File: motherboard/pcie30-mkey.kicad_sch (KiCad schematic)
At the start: 57 parts, among them IC1 PI6C557-05BLE, J15 Bus_M.2_Socket_M, U20 TPS54331DR, U21 AP2127K-3.3, Y1 25MHz

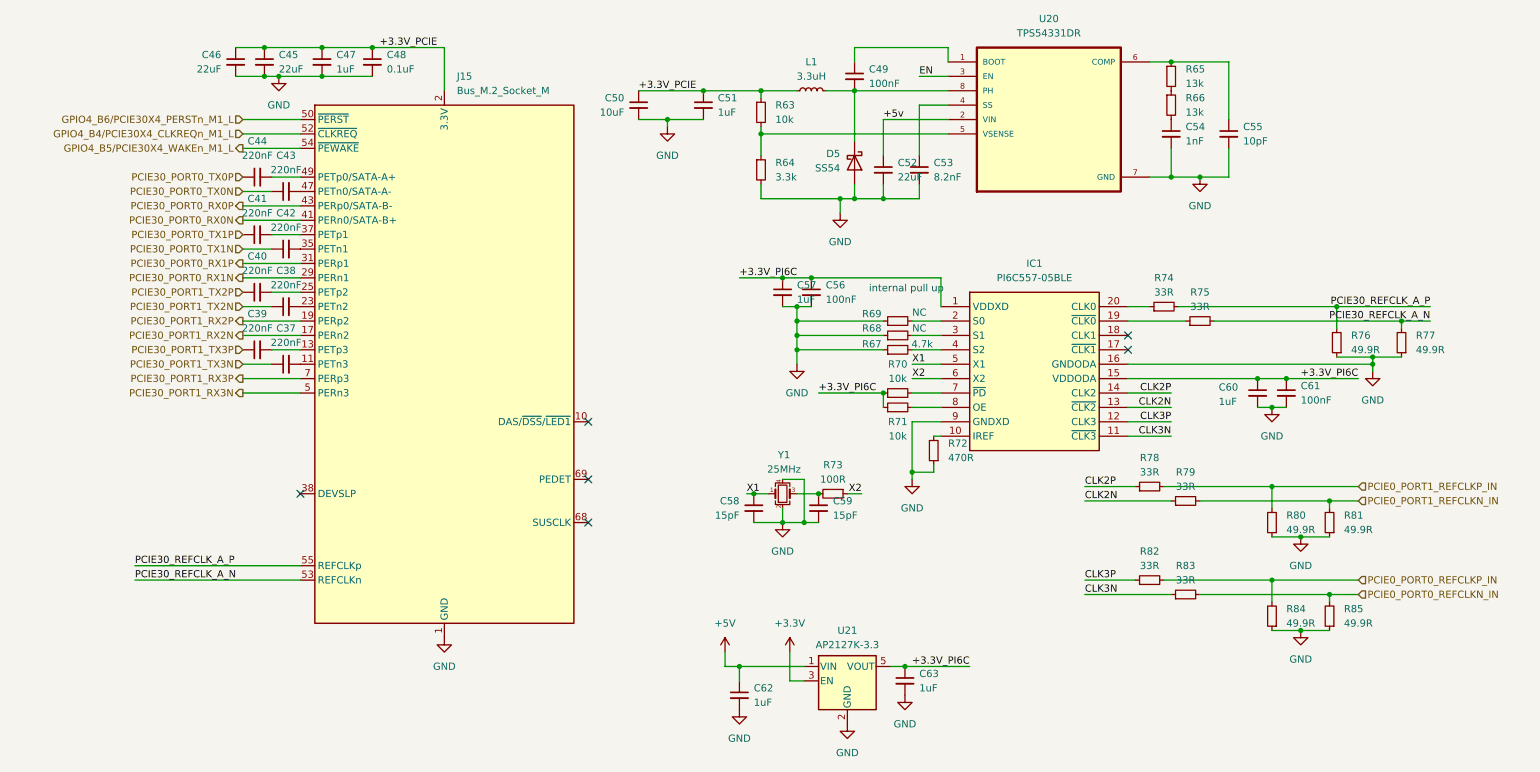
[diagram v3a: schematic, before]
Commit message: cost optimizations for jlc
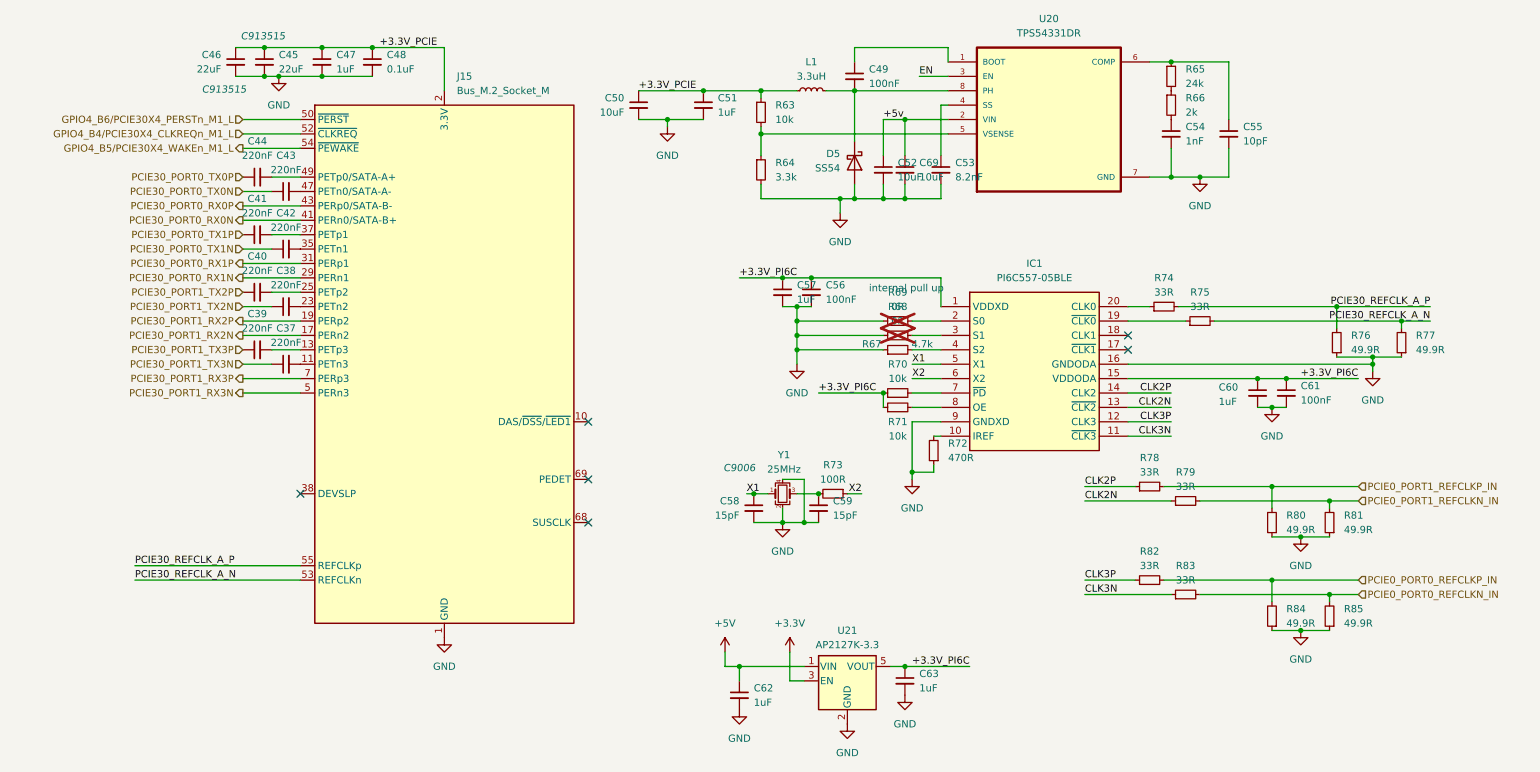
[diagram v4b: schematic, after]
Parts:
- added C69: 10uF, Capacitor_SMD:C_0402_1005Metric, symbol Device:C_Small
- C45, C46: footprint Capacitor_SMD:C_0402_1005Metric -> Capacitor_SMD:C_0603_1608Metric
- C50, C51: footprint Capacitor_SMD:C_1206_3216Metric -> Capacitor_SMD:C_0402_1005Metric
- C52: value 22uF -> 10uF; footprint Capacitor_SMD:C_0603_1608Metric -> Capacitor_SMD:C_0402_1005Metric
- C53: footprint Capacitor_SMD:C_0603_1608Metric -> Capacitor_SMD:C_0402_1005Metric
- R65: value 13k -> 24k
- R66: value 13k -> 2k
- R68, R69: value NC -> 0R; now not fitted
- Y1: footprint Crystal:Crystal_SMD_2016-4Pin_2.0x1.6mm -> Crystal:Crystal_SMD_3225-4Pin_3.2x2.5mm
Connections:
- net +5v: now also C69.1
- net GND: now also C69.2
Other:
- moved on the sheet: C53
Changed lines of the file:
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@@
 	)
 	(junction
+		(at 168.91 46.99)
+		(diameter 0)
+		(color 0 0 0 0)
+	)
+	(junction
 		(at 149.86 66.04)
 		(diameter 0)
@@
 	)
 	(junction
+		(at 168.91 33.02)
+		(diameter 0)
+		(color 0 0 0 0)
+	)
+	(junction
 		(at 139.7 129.54)
 		(diameter 0)
@@
 	(wire
 		(pts
-			(xy 176.53 30.48) (xy 171.45 30.48)
+			(xy 175.26 30.48) (xy 176.53 30.48)
 		)
 		(stroke
@@
 	(wire
 		(pts
+			(xy 168.91 44.45) (xy 168.91 46.99)
+		)
+		(stroke
+			(width 0)
+			(type default)
+		)
+	)
+	(wire
+		(pts
 			(xy 165.1 46.99) (xy 165.1 44.45)
 		)
@@
 	(wire
 		(pts
+			(xy 168.91 33.02) (xy 176.53 33.02)
+		)
+		(stroke
+			(width 0)
+			(type default)
+		)
+	)
+	(wire
+		(pts
+			(xy 168.91 33.02) (xy 168.91 39.37)
+		)
+		(stroke
+			(width 0)
+			(type default)
+		)
+	)
+	(wire
+		(pts
 			(xy 214.63 97.79) (xy 233.68 97.79)
 		)
@@
 	(wire
 		(pts
-			(xy 171.45 30.48) (xy 171.45 39.37)
+			(xy 175.26 30.48) (xy 175.26 39.37)
 		)
 		(stroke
@@
 	(wire
 		(pts
+			(xy 168.91 46.99) (xy 175.26 46.99)
+		)
+		(stroke
+			(width 0)
+			(type default)
+		)
+	)
+	(wire
+		(pts
 			(xy 160.02 36.83) (xy 160.02 27.94)
 		)
@@
 	(wire
 		(pts
-			(xy 165.1 46.99) (xy 171.45 46.99)
+			(xy 165.1 46.99) (xy 168.91 46.99)
 		)
 		(stroke
@@
 	(wire
 		(pts
-			(xy 171.45 46.99) (xy 171.45 44.45)
+			(xy 175.26 46.99) (xy 175.26 44.45)
 		)
 		(stroke
@@
 	(wire
 		(pts
-			(xy 165.1 33.02) (xy 176.53 33.02)
+			(xy 165.1 33.02) (xy 168.91 33.02)
 		)
 		(stroke
@@
 			)
 		)
-		(property "Value" "13k"
+		(property "Value" "2k"
 			(at 218.44 31.7499 0)
 			(effects
@@
 	)
 	(symbol
+		(lib_id "Device:C_Small")
+		(at 168.91 41.91 0)
+		(unit 1)
+		(exclude_from_sim no)
+		(in_bom yes)
+		(on_board yes)
+		(dnp no)
+		(property "Reference" "C69"
+			(at 171.45 40.6462 0)
+			(effects
+				(font
+					(size 1.27 1.27)
+				)
+				(justify left)
+			)
+		)
+		(property "Value" "10uF"
+			(at 171.45 43.18 0)
+			(effects
+				(font
+					(size 1.27 1.27)
+				)
+				(justify left)
+			)
+		)
+		(property "Footprint" "Capacitor_SMD:C_0402_1005Metric"
+			(at 168.91 41.91 0)
+			(effects
+				(font
+					(size 1.27 1.27)
+				)
+				(hide yes)
+			)
+		)
+		(property "Datasheet" "~"
+			(at 168.91 41.91 0)
+			(effects
+				(font
+					(size 1.27 1.27)
+				)
+				(hide yes)
+			)
+		)
+		(property "Description" "C527590"
+			(at 168.91 41.91 0)
+			(effects
+				(font
+					(size 1.27 1.27)
+				)
+				(hide yes)
+			)
+		)
+		(pin "1"
+		)
+		(pin "2"
+		)
+		(instances
+			(project "motherboard"
+				(path "/025fe4d1-0305-4b34-be04-f8d9818125a4/8b9107a7-7899-4235-bab8-96db30f71454"
+					(reference "C69")
+					(unit 1)
+				)
+			)
+		)
+	)
+	(symbol
 		(lib_id "Device:L_Small")
 		(at 152.4 27.94 90)
@@
 		(on_board yes)
 		(dnp no)
-		(fields_autoplaced yes)
 		(property "Reference" "Y1"
 			(at 147.574 92.202 0)
@@
 			)
 		)
-		(property "Footprint" "Crystal:Crystal_SMD_2016-4Pin_2.0x1.6mm"
+		(property "Footprint" "Crystal:Crystal_SMD_3225-4Pin_3.2x2.5mm"
 			(at 147.32 99.06 0)
 			(effects
@@
 			)
 		)
-		(property "Description" "Four pin crystal, GND on pins 2 and 4, small symbol"
-			(at 147.32 99.06 0)
+		(property "Description" "C9006"
+			(at 139.7 94.488 0)
 			(effects
 				(font
 					(size 1.27 1.27)
+					(italic yes)
 				)
-				(hide yes)
 			)
 		)
@@
 			)
 		)
-		(property "Footprint" "Capacitor_SMD:C_1206_3216Metric"
+		(property "Footprint" "Capacitor_SMD:C_0402_1005Metric"
 			(at 121.92 30.48 0)
 			(effects
@@
 			)
 		)
-		(property "Description" "Unpolarized capacitor, small symbol"
+		(property "Description" "C527590"
 			(at 121.92 30.48 0)
 			(effects
@@
 		(in_bom yes)
 		(on_board yes)
-		(dnp no)
+		(dnp yes)
 		(fields_autoplaced yes)
 		(property "Reference" "R68"
-			(at 163.068 69.85 90)
+			(at 167.64 66.04 90)
 			(effects
 				(font
@@
 			)
 		)
-		(property "Value" "NC"
-			(at 171.45 69.85 90)
+		(property "Value" "0R"
+			(at 167.64 68.58 90)
 			(effects
 				(font
@@
 		(on_board yes)
 		(dnp no)
-		(fields_autoplaced yes)
 		(property "Reference" "C45"
 			(at 58.42 21.5962 0)
@@
 			)
 		)
-		(property "Footprint" "Capacitor_SMD:C_0402_1005Metric"
+		(property "Footprint" "Capacitor_SMD:C_0603_1608Metric"
 			(at 55.88 22.86 0)
 			(effects
@@
 			)
 		)
-		(property "Description" "Unpolarized capacitor, small symbol"
-			(at 55.88 22.86 0)
+		(property "Description" "C913515"
+			(at 55.626 18.288 0)
 			(effects
 				(font
 					(size 1.27 1.27)
+					(italic yes)
 				)
-				(hide yes)
 			)
 		)
@@
 			)
 		)
-		(property "Value" "13k"
+		(property "Value" "24k"
 			(at 218.44 26.6699 0)
 			(effects
@@
 	(symbol
 		(lib_id "Device:C_Small")
-		(at 171.45 41.91 0)
+		(at 175.26 41.91 0)
 		(unit 1)
 		(exclude_from_sim no)
@@
 		(fields_autoplaced yes)
 		(property "Reference" "C53"
-			(at 173.99 40.6462 0)
+			(at 177.8 40.6462 0)
 			(effects
 				(font
@@
 		)
 		(property "Value" "8.2nF"
-			(at 173.99 43.1862 0)
+			(at 177.8 43.1862 0)
 			(effects
 				(font
@@
 			)
 		)
-		(property "Footprint" "Capacitor_SMD:C_0603_1608Metric"
-			(at 171.45 41.91 0)
+		(property "Footprint" "Capacitor_SMD:C_0402_1005Metric"
+			(at 175.26 41.91 0)
 			(effects
 				(font
@@
 		)
 		(property "Datasheet" "~"
-			(at 171.45 41.91 0)
+			(at 175.26 41.91 0)
 			(effects
 				(font
@@
 		)
 		(property "Description" "Unpolarized capacitor, small symbol"
-			(at 171.45 41.91 0)
+			(at 175.26 41.91 0)
 			(effects
 				(font
@@
 		(on_board yes)
 		(dnp no)
-		(fields_autoplaced yes)
 		(property "Reference" "C46"
 			(at 48.26 21.5962 0)
@@
 			)
 		)
-		(property "Footprint" "Capacitor_SMD:C_0402_1005Metric"
+		(property "Footprint" "Capacitor_SMD:C_0603_1608Metric"
 			(at 50.8 22.86 0)
 			(effects
@@
 			)
 		)
-		(property "Description" "Unpolarized capacitor, small symbol"
-			(at 50.8 22.86 0)
+		(property "Description" "C913515"
+			(at 48.768 27.686 0)
 			(effects
 				(font
 					(size 1.27 1.27)
+					(italic yes)
 				)
-				(hide yes)
 			)
 		)
@@
 		(in_bom yes)
 		(on_board yes)
-		(dnp no)
+		(dnp yes)
 		(fields_autoplaced yes)
 		(property "Reference" "R69"
-			(at 163.068 67.31 90)
+			(at 167.64 63.5 90)
 			(effects
 				(font
@@
 			)
 		)
-		(property "Value" "NC"
-			(at 171.45 67.056 90)
+		(property "Value" "0R"
+			(at 167.64 66.04 90)
 			(effects
 				(font
@@
 		(on_board yes)
 		(dnp no)
-		(fields_autoplaced yes)
 		(property "Reference" "C52"
 			(at 167.64 40.6462 0)
@@
 			)
 		)
-		(property "Value" "22uF"
-			(at 167.64 43.1862 0)
+		(property "Value" "10uF"
+			(at 167.64 43.18 0)
 			(effects
 				(font
@@
 			)
 		)
-		(property "Footprint" "Capacitor_SMD:C_0603_1608Metric"
+		(property "Footprint" "Capacitor_SMD:C_0402_1005Metric"
 			(at 165.1 41.91 0)
 			(effects
@@
 			)
 		)
-		(property "Description" "Unpolarized capacitor, small symbol"
+		(property "Description" "C527590"
 			(at 165.1 41.91 0)
 			(effects
@@
 			)
 		)
-		(property "Footprint" "Capacitor_SMD:C_1206_3216Metric"
+		(property "Footprint" "Capacitor_SMD:C_0402_1005Metric"
 			(at 133.35 30.48 0)
 			(effects

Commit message: motherboard schematic done
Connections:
- net +5v is gone; now on net +5V: C52.1, C69.1, U20.2 (VIN)
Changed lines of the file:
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@@
 	)
 	(junction
+		(at 165.1 33.02)
+		(diameter 0)
+		(color 0 0 0 0)
+	)
+	(junction
 		(at 160.02 27.94)
 		(diameter 0)
@@
 		)
 	)
-	(label "+5v"
-		(at 165.1 33.02 0)
-		(fields_autoplaced yes)
-		(effects
-			(font
-				(size 1.27 1.27)
-			)
-			(justify left bottom)
-		)
-	)
 	(label "+3.3V_PCIE"
 		(at 121.92 27.94 0)
@@
 					(unit 1)
 				)
+			)
+		)
+	)
+	(symbol
+		(lib_id "power:+5V")
+		(at 165.1 33.02 0)
+		(unit 1)
+		(exclude_from_sim no)
+		(in_bom yes)
+		(on_board yes)
+		(dnp no)
+		(fields_autoplaced yes)
+		(property "Reference" "#PWR0137"
+			(at 165.1 36.83 0)
+			(effects
+				(font
+					(size 1.27 1.27)
+				)
+				(hide yes)
+			)
+		)
+		(property "Value" "+5V"
+			(at 165.1 27.94 0)
+			(effects
+				(font
+					(size 1.27 1.27)
+				)
+			)
+		)
+		(property "Footprint" ""
+			(at 165.1 33.02 0)
+			(effects
+				(font
+					(size 1.27 1.27)
+				)
+				(hide yes)
+			)
+		)
+		(property "Datasheet" ""
+			(at 165.1 33.02 0)
+			(effects
+				(font
+					(size 1.27 1.27)
+				)
+				(hide yes)
+			)
+		)
+		(property "Description" "Power symbol creates a global label with name \"+5V\""
+			(at 165.1 33.02 0)
+			(effects
+				(font
+					(size 1.27 1.27)
+				)
+				(hide yes)
+			)
+		)
+		(pin "1"
+		)
+		(instances
+			(project ""
+				(path "/025fe4d1-0305-4b34-be04-f8d9818125a4/8b9107a7-7899-4235-bab8-96db30f71454"
+					(reference "#PWR0137")
+					(unit 1)
+				)

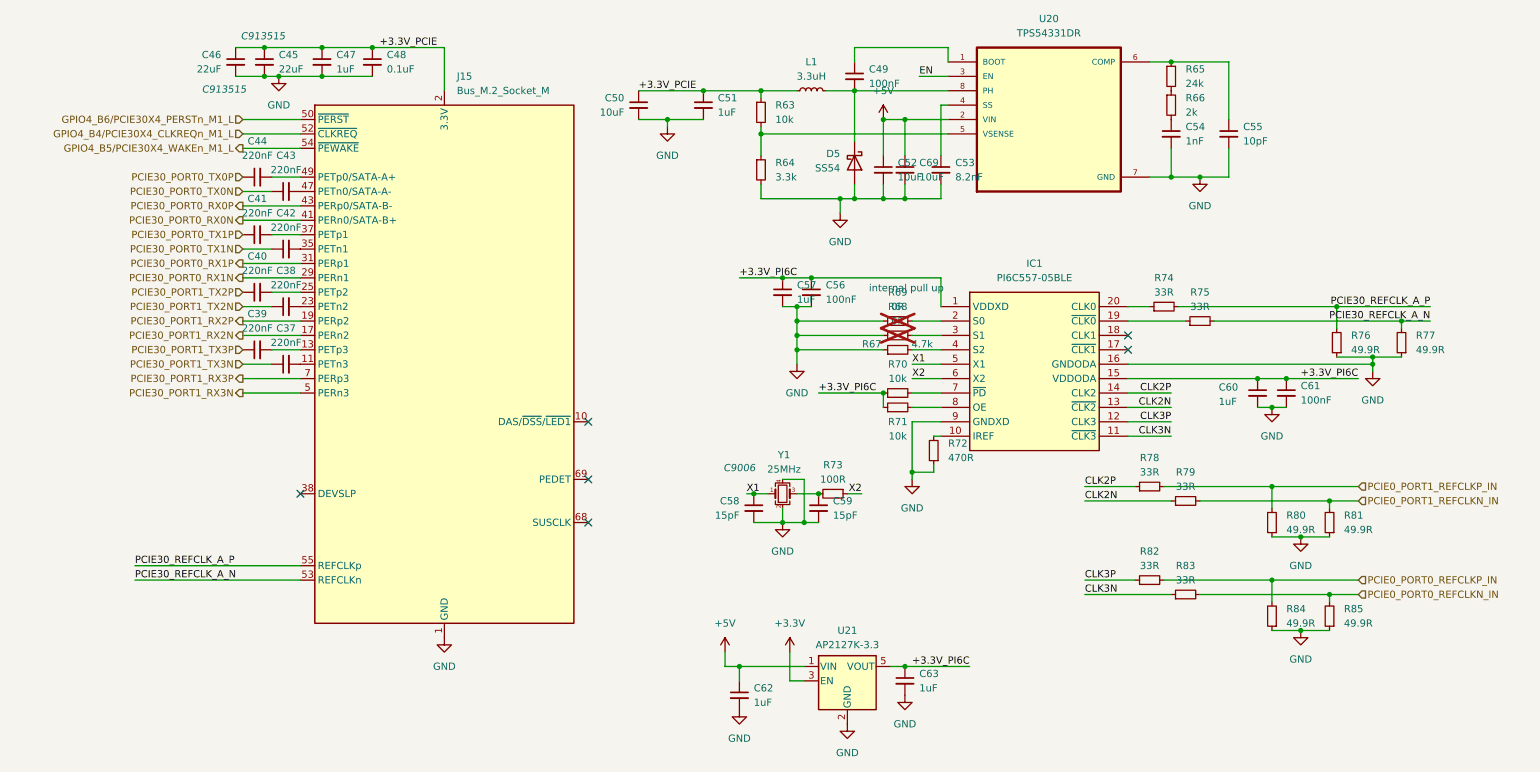
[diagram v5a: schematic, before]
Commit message: component placement of I/O
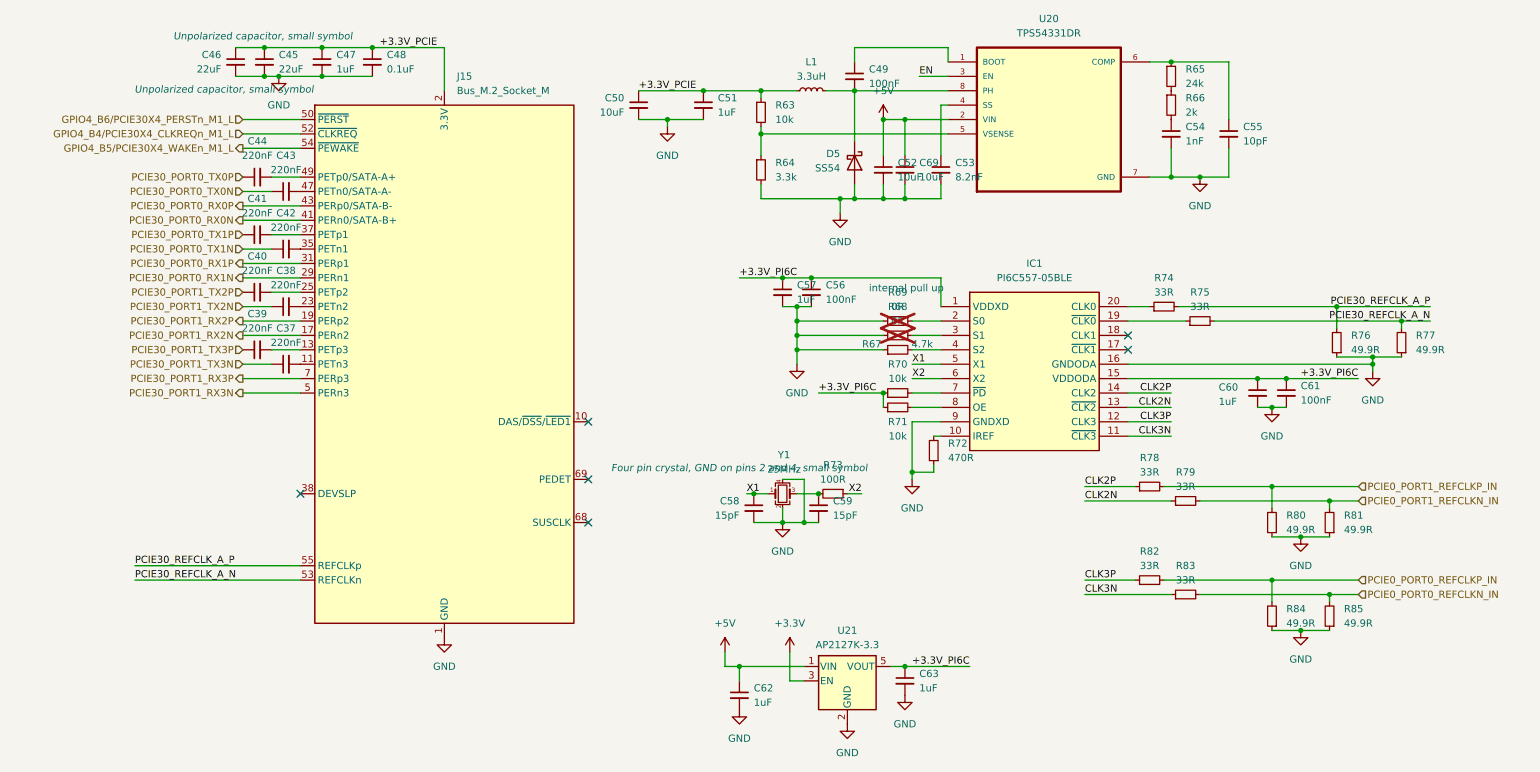
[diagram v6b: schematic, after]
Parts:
- IC1: footprint SOP65P640X120-20N:SOP65P640X120-20N -> SOP65P640X120-20N
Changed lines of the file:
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@@
 			)
 		)
-		(property "Description" "C527590"
+		(property "Description" "Unpolarized capacitor, small symbol"
 			(at 168.91 41.91 0)
 			(effects
@@
 			)
 		)
-		(property "Description" "C9006"
+		(property "Description" "Four pin crystal, GND on pins 2 and 4, small symbol"
 			(at 139.7 94.488 0)
 			(effects
@@
 			)
 		)
-		(property "Description" "C527590"
+		(property "Description" "Unpolarized capacitor, small symbol"
 			(at 121.92 30.48 0)
 			(effects
@@
 			)
 		)
-		(property "Footprint" "SOP65P640X120-20N:SOP65P640X120-20N"
+		(property "Footprint" "SOP65P640X120-20N"
 			(at 204.47 160.96 0)
 			(effects
@@
 			)
 		)
-		(property "Description" "C913515"
+		(property "Description" "Unpolarized capacitor, small symbol"
 			(at 55.626 18.288 0)
 			(effects
@@
 			)
 		)
-		(property "Description" "C913515"
+		(property "Description" "Unpolarized capacitor, small symbol"
 			(at 48.768 27.686 0)
 			(effects
@@
 			)
 		)
-		(property "Description" "C527590"
+		(property "Description" "Unpolarized capacitor, small symbol"
 			(at 165.1 41.91 0)
 			(effects
